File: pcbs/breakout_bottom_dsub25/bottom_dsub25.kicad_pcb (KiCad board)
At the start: 2 copper layers, 18 parts, among them J1 DB25_Pins, J10 f3, J11 f3, J12 f4, J16 f4, J2 Conn_01x12, J22_240V_OUT1 Screw_Terminal_01x02, J23 f2, J24 f2, J25 f1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

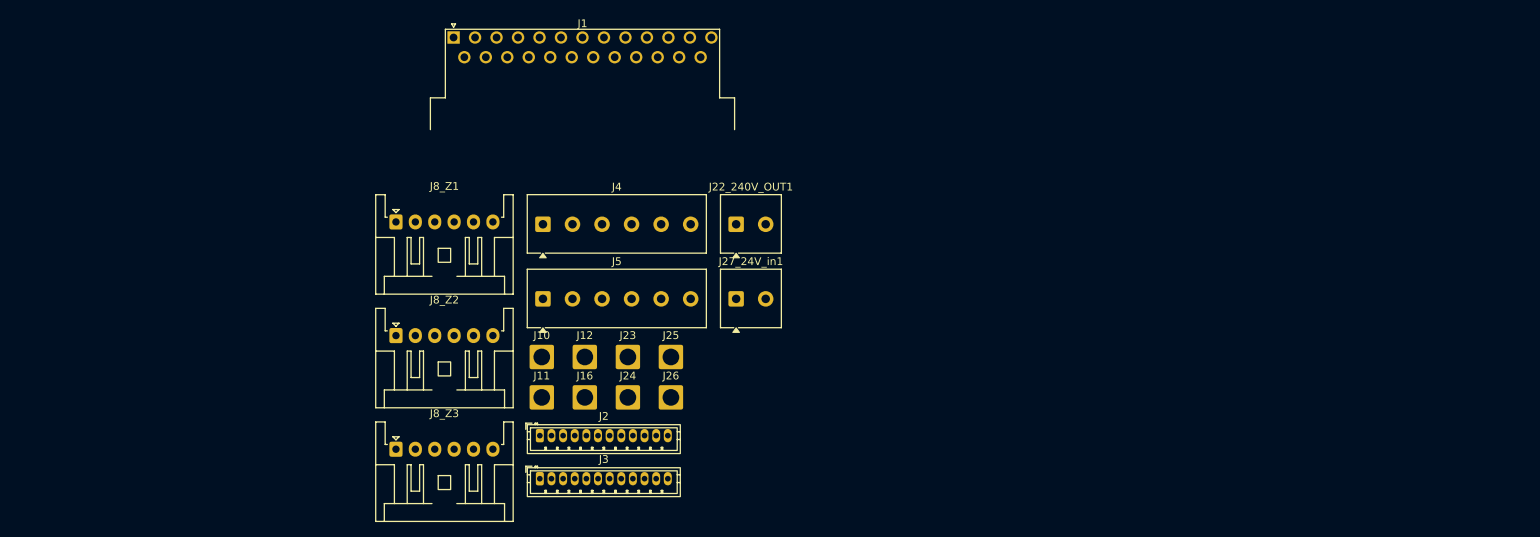
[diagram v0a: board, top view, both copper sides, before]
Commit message: rough component positioning for bottom pcb + add connectors
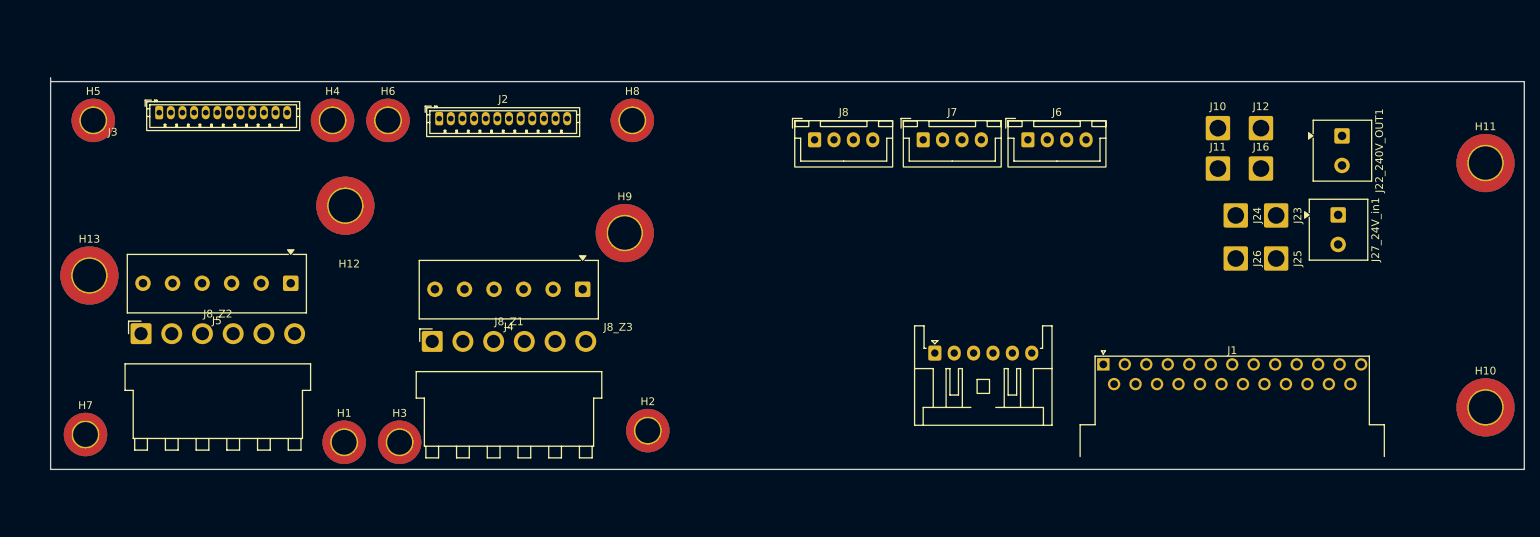
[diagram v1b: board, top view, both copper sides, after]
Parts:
- added H1: MountingHole, MountingHole:MountingHole_3.2mm_M3_DIN965_Pad_TopBottom, F.Cu at (106.8, 106.5)
- added H10: MountingHole, MountingHole:MountingHole_4.3mm_M4_DIN965_Pad_TopBottom, F.Cu at (254.0, 102.0)
- added H11: MountingHole, MountingHole:MountingHole_4.3mm_M4_DIN965_Pad_TopBottom, F.Cu at (254.0, 70.5)
- added H12: MountingHole, MountingHole:MountingHole_4.3mm_M4_DIN965_Pad_TopBottom, F.Cu at (107.0, 76.0)
- added H13: MountingHole, MountingHole:MountingHole_4.3mm_M4_DIN965_Pad_TopBottom, F.Cu at (74.0, 85.0)
- added H2: MountingHole, MountingHole:MountingHole_3.2mm_M3_DIN965_Pad_TopBottom, F.Cu at (146.0, 105.0)
- added H3: MountingHole, MountingHole:MountingHole_3.2mm_M3_DIN965_Pad_TopBottom, F.Cu at (114.0, 106.5)
- added H4: MountingHole, MountingHole:MountingHole_3.2mm_M3_DIN965_Pad_TopBottom, F.Cu at (105.3, 65.0)
- added H5: MountingHole, MountingHole:MountingHole_3.2mm_M3_DIN965_Pad_TopBottom, F.Cu at (74.5, 65.0)
- added H6: MountingHole, MountingHole:MountingHole_3.2mm_M3_DIN965_Pad_TopBottom, F.Cu at (112.5, 65.0)
- added H7: MountingHole, MountingHole:MountingHole_3.2mm_M3_DIN965_Pad_TopBottom, F.Cu at (73.5, 105.5)
- added H8: MountingHole, MountingHole:MountingHole_3.2mm_M3_DIN965_Pad_TopBottom, F.Cu at (144.0, 65.0)
- added H9: MountingHole, MountingHole:MountingHole_4.3mm_M4_DIN965_Pad_TopBottom, F.Cu at (143.0, 79.5)
- added J6: Conn_01x04, Connector_JST:JST_XH_B4B-XH-A_1x04_P2.50mm_Vertical, F.Cu at (195.0, 67.5)
- added J7: Conn_01x04, Connector_JST:JST_XH_B4B-XH-A_1x04_P2.50mm_Vertical, F.Cu at (181.5, 67.5)
- added J8: Conn_01x04, Connector_JST:JST_XH_B4B-XH-A_1x04_P2.50mm_Vertical, F.Cu at (167.5, 67.5)
- J8_Z1, J8_Z2: footprint Connector_JST:JST_XA_S06B-XASK-1_1x06_P2.50mm_Horizontal -> Connector_JST:JST_VH_B6PS-VH_1x06_P3.96mm_Horizontal
- moved J1 93.8 mm to (204.7, 96.5)
- moved J10 92.0 mm to (219.5, 66.0)
- moved J11 92.0 mm to (219.5, 71.2)
- moved J12 92.0 mm to (225.1, 66.0)
- moved J16 92.0 mm to (225.1, 71.2)
- moved J23 85.6 mm to (227.0, 77.3), turned to -90 degrees
- moved J24 81.8 mm to (221.8, 77.3), turned to -90 degrees
- moved J25 79.1 mm to (227.0, 82.8), turned to -90 degrees
- moved J22_240V_OUT1 78.9 mm to (235.5, 67.0), turned to -90 degrees
- moved J27_24V_in1 78.4 mm to (235.0, 77.2), turned to -90 degrees
- moved J26 75.0 mm to (221.8, 82.8), turned to -90 degrees
- moved J8_Z3 70.6 mm to (183.0, 95.0)
- moved J3 68.1 mm to (83.0, 64.0)
- moved J2 42.9 mm to (119.1, 64.8)
- moved J8_Z2 32.9 mm to (80.7, 92.5)
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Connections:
- J1 pad 17: unconnected-(J1-P17-Pad17) -> Net-(J1-P17)
- J1 pad 18: unconnected-(J1-P18-Pad18) -> Net-(J1-P18)
- J1 pad 19: unconnected-(J1-P19-Pad19) -> Net-(J1-P19)
- J1 pad 20: unconnected-(J1-P20-Pad20) -> Net-(J1-P20)
- J1 pad 21: unconnected-(J1-P21-Pad21) -> Net-(J1-P21)
- J1 pad 4: unconnected-(J1-Pad4) -> Net-(J8-Pin_2)
- J1 pad 5: unconnected-(J1-Pad5) -> Net-(J8-Pin_4)
- J1 pad 6: unconnected-(J1-Pad6) -> Net-(J7-Pin_2)
- J1 pad 7: unconnected-(J1-Pad7) -> Net-(J7-Pin_4)
- J1 pad 8: unconnected-(J1-Pad8) -> Net-(J6-Pin_2)
- J1 pad 9: unconnected-(J1-Pad9) -> Net-(J6-Pin_4)
- J2 pad 1: Net-(J1-P25) -> unconnected-(J2-Pin_1-Pad1)
- J2 pad 2: unconnected-(J2-Pin_2-Pad2) -> Net-(J1-P25)
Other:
- board outline added: 190 x 50.5 mm

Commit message: add routinng
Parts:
- removed J10, J11: f3, Connector_Wire:SolderWire-1.5sqmm_1x01_D1.7mm_OD3mm
- removed J12, J16: f4, Connector_Wire:SolderWire-1.5sqmm_1x01_D1.7mm_OD3mm
- removed J22_240V_OUT1, J27_24V_in1: Screw_Terminal_01x02, TerminalBlock_Phoenix:TerminalBlock_Phoenix_MKDS-1-2-3.81_1x02_P3.81mm_Horizontal
- removed J23, J24: f2, Connector_Wire:SolderWire-1.5sqmm_1x01_D1.7mm_OD3mm
- removed J25, J26: f1, Connector_Wire:SolderWire-1.5sqmm_1x01_D1.7mm_OD3mm
- removed J6: Conn_01x04, Connector_JST:JST_XH_B4B-XH-A_1x04_P2.50mm_Vertical
- J1: footprint Connector_Dsub:DSUB-25_Pins_Horizontal_P2.77x2.54mm_EdgePinOffset9.40mm -> Connector_Dsub:DSUB-25_Pins_Vertical_P2.77x2.84mm_MountingHoles
- J8_Z1, J8_Z2: footprint Connector_JST:JST_VH_B6PS-VH_1x06_P3.96mm_Horizontal -> Connector_JST:JST_VH_B6P-VH_1x06_P3.96mm_Vertical
- J8_Z3: footprint Connector_JST:JST_XA_S06B-XASK-1_1x06_P2.50mm_Horizontal -> Connector_JST:JST_XA_B06B-XASK-1_1x06_P2.50mm_Vertical
- moved J2 48.9 mm to (168.0, 65.5), turned to 180 degrees
- moved J8 43.0 mm to (210.5, 65.5), turned to 180 degrees
- moved H9 36.6 mm to (179.5, 83.0)
- moved H8 33.0 mm to (177.0, 63.5)
- moved H2 31.0 mm to (177.0, 105.5)
- moved J3 24.0 mm to (107.0, 65.5), turned to 180 degrees
- moved J8_Z3 22.1 mm to (161.0, 93.0), turned to 90 degrees
- moved J7 15.1 mm to (196.5, 65.5), turned to 180 degrees
- moved H6 14.5 mm to (126.9, 63.5)
- moved H3 13.0 mm to (127.0, 105.5)
- moved H4 12.7 mm to (118.0, 63.5)
- moved H1 11.2 mm to (118.0, 105.5)
- moved J1 7.85 mm to (212.6, 96.4), turned to 180 degrees
- moved H12 7.43 mm to (104.5, 83.0)
- moved H10 7.02 mm to (254.5, 95.0)
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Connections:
- J1 pad 10: Net-(J3-Pin_7) -> Net-(J2-Pin_3)
- J1 pad 11: Net-(J2-Pin_8) -> Net-(J2-Pin_5)
- J1 pad 12: Net-(J2-Pin_6) -> Net-(J2-Pin_7)
- J1 pad 13: Net-(J3-Pin_2) -> GND
- J1 pad 8: Net-(J6-Pin_2) -> Net-(J3-Pin_7)
- J1 pad 9: Net-(J6-Pin_4) -> Net-(J3-Pin_2)
- J2 pad 2: Net-(J1-P25) -> Net-(J1-P22)
- J2 pad 4: Net-(J2-Pin_4) -> Net-(J1-P23)
- J2 pad 6: Net-(J2-Pin_6) -> Net-(J1-P24)
- J2 pad 7: Net-(J1-P24) -> Net-(J2-Pin_7)
- J2 pad 8: Net-(J2-Pin_8) -> Net-(J1-P25)
- J2 pad 9: unconnected-(J2-Pin_9-Pad9) -> GND
- J3 pad 4: Net-(J2-Pin_4) -> Net-(J1-P23)
- J3 pad 6: Net-(J1-P23) -> Net-(J1-P21)
- J3 pad 8: Net-(J1-P22) -> Net-(J1-P20)
- J3 pad 9: unconnected-(J3-Pin_9-Pad9) -> GND
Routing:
- net Net-(J1-P20): track 0.00 -> 125.9 mm
- net Net-(J1-P21): track 0.00 -> 120.1 mm
- net Net-(J3-Pin_7): track 0.00 -> 119.8 mm
- net GND: track 0.00 -> 113.6 mm
- net Net-(J3-Pin_2): track 0.00 -> 108.2 mm
- net Net-(J2-Pin_3): track 0.00 -> 107.8 mm
- net Net-(J2-Pin_5): track 0.00 -> 106.0 mm
- net Net-(J1-P23): track 0.00 -> 105.8 mm
- net Net-(J8_Z3-Pin_6): track 0.00 -> 61.9 mm
- net Net-(J8_Z3-Pin_4): track 0.00 -> 56.6 mm
- net Net-(J1-P14): track 0.00 -> 56.6 mm
- net Net-(J8_Z3-Pin_2): track 0.00 -> 52.8 mm
- net Net-(J1-P15): track 0.00 -> 51.6 mm
- net Net-(J1-P16): track 0.00 -> 48.5 mm
- net Net-(J1-P22): track 0.00 -> 41.1 mm
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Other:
- board size 190 x 50.5 mm -> 194.5 x 50 mm

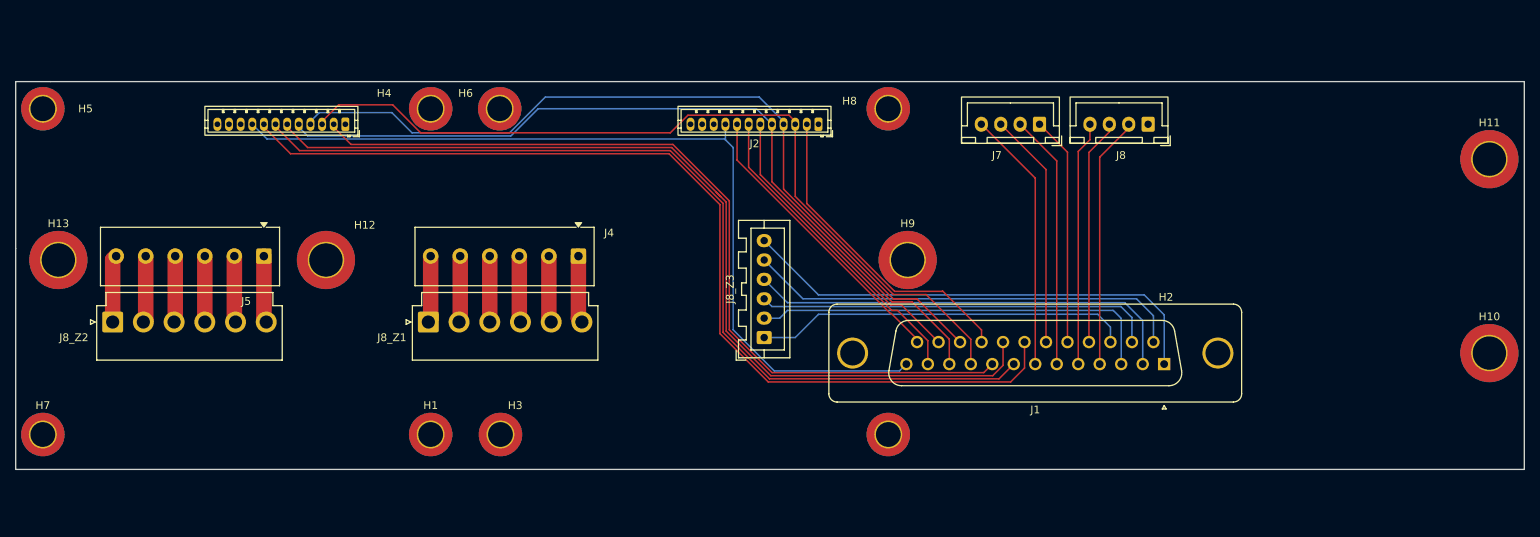
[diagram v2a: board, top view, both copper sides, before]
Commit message: adding various silk layer labels
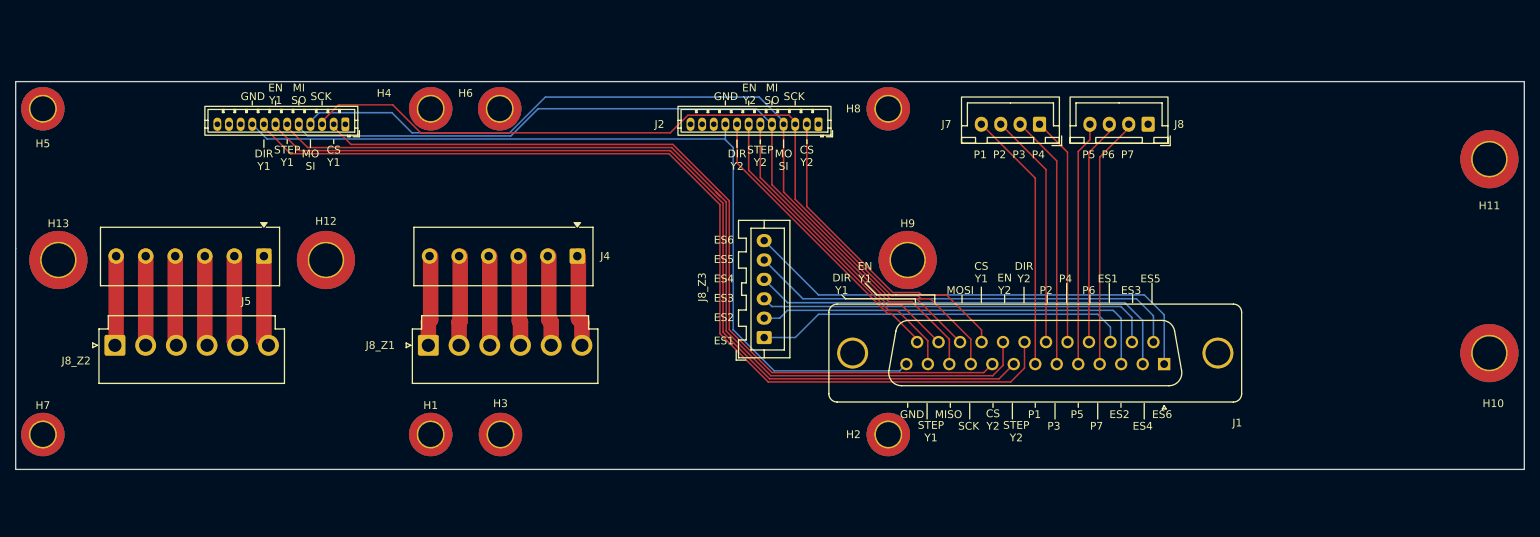
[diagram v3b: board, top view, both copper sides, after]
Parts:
- moved J8_Z2 3.01 mm to (77.3, 94.0)
- moved J8_Z1 3.00 mm to (117.7, 94.0)
- moved J4 0.14 mm to (136.9, 82.5)
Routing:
- net Net-(J5-Pin_3): track 8.50 -> 11.6 mm
- net Net-(J5-Pin_1): track 8.62 -> 11.7 mm
- net Net-(J5-Pin_2): track 8.56 -> 11.7 mm
- net Net-(J4-Pin_6): track 8.62 -> 11.6 mm
- net Net-(J4-Pin_5): track 8.56 -> 11.6 mm
- net Net-(J4-Pin_4): track 8.50 -> 11.5 mm
- net Net-(J4-Pin_3): track 8.56 -> 11.6 mm
- net Net-(J4-Pin_1): track 8.69 -> 11.7 mm
- net Net-(J4-Pin_2): track 8.62 -> 11.6 mm
- net Net-(J5-Pin_4): track 8.56 -> 11.6 mm
- net Net-(J5-Pin_6): track 8.69 -> 11.6 mm
- net Net-(J5-Pin_5): track 8.62 -> 11.5 mm
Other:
- board text added: "CS Y1"
- board text added: "CS Y2"
- board text added: "DIR Y1"
- board text added: "DIR Y2"
- board text added: "EN Y1"
- board text added: "EN Y2"
- board text added: "ES1"
- board text added: "ES2"
- board text added: "ES3"
- board text added: "ES4"
- board text added: "ES5"
- board text added: "ES6"
- board text added: "GND"
- board text added: "MI SO"
- board text added: "MISO"
- board text added: "MO SI"
- board text added: "MOSI"
- board text added: "P1"
- board text added: "P2"
- board text added: "P3"
- board text added: "P4"
- board text added: "P5"
- board text added: "P6"
- board text added: "P7"
- board text added: "SCK"
- board text added: "STEP Y1"
- board text added: "STEP Y2"

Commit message: adding ground plan
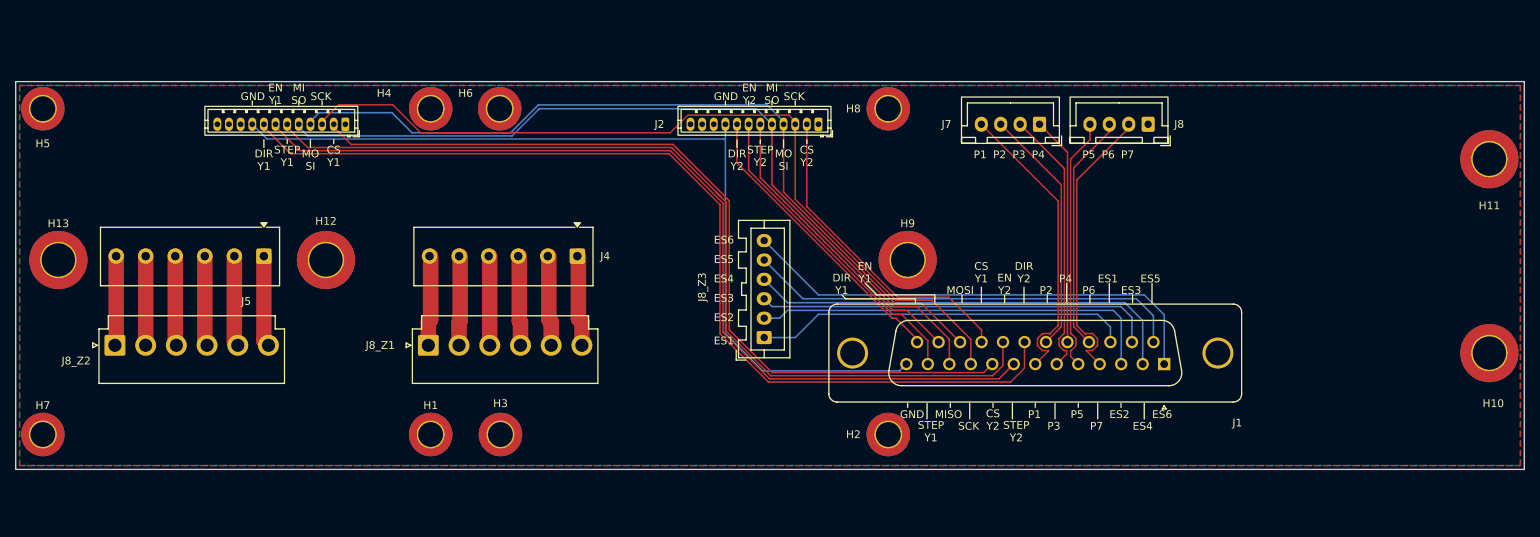
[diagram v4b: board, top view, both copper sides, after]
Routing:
- net Net-(J7-Pin_4): track 33.8 -> 38.5 mm
- net Net-(J8-Pin_2): track 32.5 -> 37.2 mm
- net Net-(J7-Pin_2): track 32.9 -> 34.8 mm
- net Net-(J1-P19): track 30.5 -> 32.1 mm
- net Net-(J1-P17): track 29.2 -> 30.8 mm
- net Net-(J8-Pin_4): track 31.5 -> 33.0 mm
- net GND: track 113.6 -> 114.5 mm
- net Net-(J1-P23): track 106.0 -> 105.2 mm
- added copper zone on B.Cu, net (none)
- added copper zone on F.Cu, net GND

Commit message: add version/name
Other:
- board text added: "YetiCNC Revival - Bottom - v0.1 Kakwalab © - 2026"
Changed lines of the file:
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@@
+		)
+	)
+	(gr_text "YetiCNC Revival - Bottom - v0.1\nKakwalab © - 2026"
+		(at 89 105.5 0)
+		(layer "F.SilkS")
+		(effects
+			(font
+				(size 1.27 1.27)
+			)
 		)
 	)

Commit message: wire-in the 24V from the main board + wire ground on this pin
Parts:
- removed J8: Conn_01x04, Connector_JST:JST_XH_B4B-XH-A_1x04_P2.50mm_Vertical
- added J6: Conn_01x02, Connector_JST:JST_XH_B2B-XH-A_1x02_P2.50mm_Vertical, F.Cu at (208.0, 65.6)
- moved J8_Z1 14.5 mm to (132.2, 94.5)
- moved J4 14.5 mm to (151.4, 83.0)
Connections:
- J1 pad 5: Net-(J8-Pin_4) -> Net-(J7-Pin_1)
- J1 pad 6: Net-(J7-Pin_2) -> Net-(J7-Pin_3)
- J1 pad 7: Net-(J7-Pin_4) -> Net-(J2-Pin_11)
- J2 pad 11: unconnected-(J2-Pin_11-Pad11) -> Net-(J2-Pin_11)
- J2 pad 12: unconnected-(J2-Pin_12-Pad12) -> GND
- J3 pad 11: unconnected-(J3-Pin_11-Pad11) -> Net-(J2-Pin_11)
- J3 pad 12: unconnected-(J3-Pin_12-Pad12) -> GND
- J7 pad 1: Net-(J1-P18) -> Net-(J7-Pin_1)
- J7 pad 2: Net-(J7-Pin_2) -> Net-(J1-P18)
- J7 pad 3: Net-(J1-P19) -> Net-(J7-Pin_3)
- J7 pad 4: Net-(J7-Pin_4) -> Net-(J1-P19)
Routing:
- net Net-(J2-Pin_11): track 0.00 -> 136.0 mm, vias 0 -> 1
- net Net-(J7-Pin_4): track 38.5 -> 0.00 mm
- net Net-(J7-Pin_2): track 34.8 -> 0.00 mm
- net Net-(J7-Pin_3): track 0.00 -> 34.7 mm
- net Net-(J8-Pin_4): track 33.0 -> 0.00 mm
- net Net-(J7-Pin_1): track 0.00 -> 33.0 mm
- net GND: track 114.5 -> 122.5 mm
- net Net-(J6-Pin_1): track 37.2 -> 34.9 mm
- net Net-(J1-P19): track 32.1 -> 33.4 mm
- net Net-(J1-P18): track 29.6 -> 30.6 mm
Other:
- board text added: "24V"
- board text added: "YetiCNC Revival - Bottom - v0.2 Kakwalab © - 2026"
- board text removed: "P7"
- board text removed: "YetiCNC Revival - Bottom - v0.1 Kakwalab © - 2026"

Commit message: bottom PCBs, correct hole placement + grounded plane + remove warnings
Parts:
- moved H10 5.00 mm to (254.5, 100.0)
- moved H11 5.00 mm to (254.5, 75.0)
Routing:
- net GND: track 122.5 -> 124.8 mm, vias 0 -> 11
- net Net-(J8_Z3-Pin_6): track 61.9 -> 63.8 mm
- net Net-(J2-Pin_11): track 136.0 -> 137.5 mm, vias 1 -> 2
- net Net-(J1-P16): track 48.5 -> 49.5 mm
- net Net-(J1-P14): track 56.6 -> 57.4 mm
- added copper zone on B.Cu, net GND
- removed copper zone on B.Cu, net (none)
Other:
- board text added: "YetiCNC Revival - Bottom - v0.3 Kakwalab © - 2026"
- board text removed: "YetiCNC Revival - Bottom - v0.2 Kakwalab © - 2026"
